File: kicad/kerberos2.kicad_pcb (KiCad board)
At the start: 2 copper layers, 62.5 x 83.8 mm, 212 parts, among them J1 5V, J10 rp_spare3, J11 rp_spare4, J12 rp_spare5, J13 rp_spare6, J14 503398-1892, J15 fpga_spare, J16 MIDI-in, J17 MIDI-thru, J18 MIDI-out, J19 IEC, J2 3.3V, J20 IEC, J21 IEC, J3 1.2V, J4 GND, J5 SWCLK, J6 SWD, J7 xout, J8 rp_spare1, J9 rp_spare2, Q1 Q_NMOS_GSD, Q10 Q_NMOS_GSD, Q11 Q_NMOS_GSD, Q12 Q_NMOS_GSD, Q13 Q_NMOS_GSD, Q2 Q_NMOS_GSD, Q3 Q_NMOS_GSD, Q4 Q_NMOS_GSD, Q5 Q_NMOS_GSD, Q6 Q_NMOS_GSD, Q7 Q_NMOS_GSD, Q8 Q_NMOS_GSD, Q9 Q_NMOS_GSD, SW1 side-button, SW2 SKRPADE010, U1 MX25L25645G, U10 M3406, U11 6N138, U12 74LS14, U2 MX25L25645G, U3 RP2040, U4 74ALVC164245DGG,51, U5 74ALVC164245DGG,51, U6 GW1NR-4&4B_QN881, U7 AD8694ARZ, U8 TMCS1108A3UQDR, U9 M3406, X1 SX3M12.000M20F30TNN

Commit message: circuit improvements fixed the level shifter circuit, added the shield pins to the reset button, and replaced the IEC circuit with unused pins of the 16 bit level shifter, and a new 6 channel open collector driver
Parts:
- removed the J10 at (202.5, 98.7)
- removed the J15 at (236.5, 103.2)
- removed the J19 at (163.3, 110.2)
- removed the J20 at (180.6, 110.2)
- removed the J21 at (197.9, 107.3)
- removed the J8 at (197.9, 98.7)
- removed Q1, Q10, Q11, Q12, Q13, Q2, Q3, Q4, Q5, Q6, Q7, Q8, Q9: Q_NMOS_GSD, Package_DFN_QFN:Diodes_DFN1006-3
- removed the R10 at (90.8, 28.9)
- removed the R11 at (95.5, 24.7)
- removed the R12 at (95.5, 21.8)
- removed the R17 at (99.9, 21.8)
- removed the R18 at (104.0, 27.6)
- removed the R19 at (108.7, 24.7)
- removed the R20 at (99.6, 30.6)
- removed the R21 at (95.2, 27.6)
- removed the R22 at (108.7, 21.8)
- removed the R28 at (178.0, 97.5)
- removed the R29 at (178.0, 91.5)
- removed the R30 at (182.4, 97.4)
- removed the R31 at (167.7, 102.1)
- removed the R32 at (182.4, 94.5)
- removed the R34 at (178.0, 88.6)
- removed the R38 at (216.1, 94.5)
- removed the R39 at (216.3, 91.5)
- removed the R40 at (211.7, 93.2)
- removed the R41 at (207.1, 97.9)
- removed the R42 at (216.3, 88.6)
- removed the R43 at (211.5, 97.9)
- removed R59, R74, R75, R76, R77, R78, R79, R80, R81, R82, R83, R85, R87, R89, R91, R93: 10k, Resistor_SMD:R_0805_2012Metric
- removed R72: 1k8, Resistor_SMD:R_0805_2012Metric
- removed R73: 3k3, Resistor_SMD:R_0805_2012Metric
- removed R84, R88, R92: 27, Resistor_SMD:R_0805_2012Metric
- removed R86, R90, R94: 22k, Resistor_SMD:R_0805_2012Metric
- added C18: 100n, Capacitor_SMD:C_0805_2012Metric, F.Cu at (1.70, 34.0)
- added C19: 100n, Capacitor_SMD:C_0805_2012Metric, F.Cu at (-8.13, 36.2)
- added C35: 100n, Capacitor_SMD:C_0805_2012Metric, F.Cu at (-2.75, 34.0)
- added C36: 100n, Capacitor_SMD:C_0805_2012Metric, F.Cu at (-12.6, 36.2)
- added J14: rp_spare4, Connector_PinHeader_2.54mm:PinHeader_1x01_P2.54mm_Vertical, F.Cu at (137.2, 18.4)
- added J2: IEC_ATN, Connector_PinHeader_2.54mm:PinHeader_1x01_P2.54mm_Vertical, F.Cu at (33.6, 23.4)
- added J3: IEC_SRQ, Connector_PinHeader_2.54mm:PinHeader_1x01_P2.54mm_Vertical, F.Cu at (29.0, 23.4)
- added J4: IEC_CLK, Connector_PinHeader_2.54mm:PinHeader_1x01_P2.54mm_Vertical, F.Cu at (24.3, 23.4)
- added J5: IEC_DAT, Connector_PinHeader_2.54mm:PinHeader_1x01_P2.54mm_Vertical, F.Cu at (29.0, 28.0)
- added J6: GND, Connector_PinHeader_2.54mm:PinHeader_1x01_P2.54mm_Vertical, F.Cu at (24.3, 28.0)
- added LOGO1: logo, Symbol:WEEE-Logo_4.2x6mm_SilkScreen, F.Cu at (86.0, 43.1)
- added LOGO2: logo, Symbol:CE-Logo_8.5x6mm_SilkScreen, F.Cu at (67.4, 42.5)
- added R3: 3k3, Resistor_SMD:R_0805_2012Metric, F.Cu at (42.6, 22.5)
- added R36: NA, Resistor_SMD:R_0805_2012Metric, F.Cu at (147.9, 27.4)
- added R37: 10k, Resistor_SMD:R_0805_2012Metric, F.Cu at (127.8, 30.8)
- added R4: 3k3, Resistor_SMD:R_0805_2012Metric, F.Cu at (24.2, 31.8)
- added R5: 3k3, Resistor_SMD:R_0805_2012Metric, F.Cu at (37.9, 28.4)
- added R6: 3k3, Resistor_SMD:R_0805_2012Metric, F.Cu at (33.5, 27.2)
- added U4: 74LCX16245, SOP50:SOP50P810X120-48N, F.Cu at (93.2, 99.5)
- added U8: 74LS06, Package_SO:SO-14_3.9x8.65mm_P1.27mm, F.Cu at (-0.75, 26.8)
- added U9: 74LS06, Package_SO:SO-14_3.9x8.65mm_P1.27mm, F.Cu at (7.70, 26.8)
- J11: value rp_spare4 -> rp_spare1
- J12: value rp_spare5 -> rp_spare2
- J13: value rp_spare6 -> rp_spare3
- J9: value rp_spare2 -> current-measurement
- R23, R24, R25, R26, R27, R33: value 27 -> 10k
- SW1: value side-button -> side-switch
- U1: moved to B.Cu
- U5: renamed from U4; value 74ALVC164245DGG,51 -> 74LCX16245; footprint Package_SO:TSSOP-48_8x12.5mm_P0.5mm -> SOP50:SOP50P810X120-48N
- U7: renamed from U5; value 74ALVC164245DGG,51 -> 74LCX16245; footprint Package_SO:TSSOP-48_8x12.5mm_P0.5mm -> SOP50:SOP50P810X120-48N
- moved R25 198.2 mm to (-3.70, 37.0)
- moved R27 188.9 mm to (0.71, 37.0)
- moved R26 187.1 mm to (14.1, 22.5)
- moved R23 178.9 mm to (14.1, 25.5)
- moved R24 178.1 mm to (6.13, 34.0)
- moved R15 159.8 mm to (28.6, 31.8)
- moved J11 109.6 mm to (127.9, 18.4)
- moved U2 97.2 mm to (75.7, 61.9)
- moved J12 96.5 mm to (132.6, 18.4)
- moved J13 96.4 mm to (132.6, 23.1)
- moved C10 89.7 mm to (134.4, 119.1)
- moved C15 89.7 mm to (134.4, 116.1)
- moved C5 89.7 mm to (121.0, 123.4)
- moved C7 89.7 mm to (121.0, 120.4)
- moved C8 89.7 mm to (125.4, 123.3)
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- renumbered C3 to C2, C19 to C20, C20 to C24, C18 to C25, C25 to C26, C2 to C3, C24 to C30, C26 to C31, C30 to C32, C31 to C33, C32 to C34, C33 to C37, C34 to C38, C35 to C39, C36 to C40, C37 to C41, C38 to C42, C39 to C43, C40 to C44, C41 to C45, C42 to C46, C43 to C47, J4 to J10, J5 to J15, J6 to J16, J7 to J17, J14 to J18, J16 to J19, J17 to J20, J18 to J21, J2 to J7, J3 to J8, R5 to R10, R6 to R11, R3 to R12, R9 to R17, R35 to R18, R36 to R19, R37 to R20, R44 to R21, R45 to R22, R46 to R28, R47 to R29, R49 to R30, R50 to R31, R48 to R32, R51 to R34, R52 to R35, R53 to R38, R54 to R39, R55 to R40, R56 to R41, R57 to R42, R58 to R43, R60 to R44, R61 to R45, R62 to R46, R63 to R47, R64 to R48, R65 to R49, R66 to R50, R67 to R51, R68 to R52, R69 to R53, R70 to R54, R71 to R55, R4 to R7, R7 to R8, R8 to R9, U7 to U10, U8 to U11, U9 to U12, U10 to U13, U11 to U14, U12 to U15
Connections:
- J18 pad 1: Net-(J14-Pad1) -> Net-(J18-Pad1)
- J18 pad 10: Net-(J14-Pad10) -> Net-(J18-Pad10)
- J18 pad 2: Net-(J14-Pad2) -> Net-(J18-Pad2)
- J18 pad 3: Net-(J14-Pad3) -> Net-(J18-Pad3)
- J18 pad 5: Net-(J14-Pad5) -> Net-(J18-Pad5)
- J18 pad 7: Net-(J14-Pad7) -> Net-(J18-Pad7)
- J18 pad 8: Net-(J14-Pad8) -> Net-(J18-Pad8)
- J9 pad 1: Net-(J9-Pad1) -> /current sense/Vout
- JP9 pad 1: Net-(JP9-Pad1) -> GND
- JP9 pad 2: GND -> Net-(JP9-Pad2)
- R13 pad 1: /RP2040 microcontroller/spare5 -> Net-(J2-Pad1)
- R13 pad 2: /GW1NR FPGA/spare5 -> /GW1NR FPGA/IEC_ATN
- R14 pad 1: /RP2040 microcontroller/spare6 -> Net-(J3-Pad1)
- R14 pad 2: /GW1NR FPGA/spare6 -> /GW1NR FPGA/IEC_SRQ
- R15 pad 1: /RP2040 microcontroller/spare7 -> Net-(J4-Pad1)
- R15 pad 2: /GW1NR FPGA/spare7 -> /GW1NR FPGA/IEC_CLK
- R16 pad 1: /RP2040 microcontroller/JTAGSEL_N -> Net-(J5-Pad1)
- R16 pad 2: /GW1NR FPGA/JTAGSEL_N -> /GW1NR FPGA/IEC_DAT
- R18 pad 2: Net-(R31-Pad2) -> /GW1NR FPGA/FLASH-CS
- R19 pad 2: Net-(R36-Pad2) -> Net-(R19-Pad2)
- R21 pad 2: Net-(JP9-Pad1) -> Net-(JP9-Pad2)
- R22 pad 1: Net-(J14-Pad10) -> Net-(J18-Pad10)
- R23 pad 1: /RP2040 microcontroller/FLASH-SIO1 -> GND
- R24 pad 1: /RP2040 microcontroller/FLASH-SIO0 -> GND
- R25 pad 1: /RP2040 microcontroller/FLASH-SCLK -> GND
- R26 pad 1: /RP2040 microcontroller/FLASH-CS -> GND
- R27 pad 1: /RP2040 microcontroller/FLASH-SIO2 -> GND
- R33 pad 1: /GW1NR FPGA/FLASH-SIO3 -> +3.3V
- R33 pad 2: Net-(R33-Pad2) -> /GW1NR FPGA/FLASH-SIO3
- R34 pad 1: Net-(R51-Pad1) (its old number) -> GND
- R34 pad 2: GND -> Net-(R34-Pad2)
- R35 pad 1: Net-(R52-Pad1) (its old number) -> GND
- R35 pad 2: GND -> Net-(R35-Pad2)
- RN1 pad 1: Net-(JP1-Pad8) -> Net-(JP1-Pad4)
- RN1 pad 10: /~{DMA} -> I/O2
- RN1 pad 11: /BA -> ~{EXROM}
- RN1 pad 12: /~{IRQ} -> ~{GAME}
- RN1 pad 13: /R/W -> I/O1
- RN1 pad 14: /DOT-CLK -> DOT-CLK
- RN1 pad 15: /I/O1 -> R/W
- RN1 pad 16: /~{GAME} -> ~{IRQ}
- RN1 pad 2: Net-(JP1-Pad7) -> Net-(JP1-Pad5)
- RN1 pad 4: Net-(JP1-Pad5) -> Net-(JP1-Pad7)
- RN1 pad 5: Net-(JP1-Pad4) -> Net-(JP1-Pad8)
- RN1 pad 6: Net-(JP1-Pad12) -> Net-(JP1-Pad9)
- RN1 pad 7: Net-(JP1-Pad13) -> Net-(JP1-Pad10)
- RN1 pad 8: Net-(JP1-PadE) -> Net-(JP1-Pad11)
- RN1 pad 9: /S02 -> ~{ROML}
- RN2 pad 1: unconnected-(RN2-Pad1) -> Net-(JP1-Pad12)
- RN2 pad 10: /I/O2 -> unconnected-(RN2-Pad10)
- RN2 pad 11: /~{ROML} -> S02
- RN2 pad 12: /~{ROMH} -> ~{NMI}
- RN2 pad 13: /~{RESET} -> ~{RESET}
- RN2 pad 14: /~{NMI} -> ~{ROMH}
- RN2 pad 15: unconnected-(RN2-Pad15) -> ~{DMA}
- RN2 pad 16: unconnected-(RN2-Pad16) -> BA
- RN2 pad 2: unconnected-(RN2-Pad2) -> Net-(JP1-Pad13)
- RN2 pad 3: Net-(JP1-PadD) -> Net-(JP1-PadB)
- RN2 pad 5: Net-(JP1-PadB) -> Net-(JP1-PadD)
- RN2 pad 6: Net-(JP1-Pad11) -> Net-(JP1-PadE)
- RN2 pad 7: Net-(JP1-Pad10) -> unconnected-(RN2-Pad7)
- RN2 pad 8: Net-(JP1-Pad9) -> unconnected-(RN2-Pad8)
- RN2 pad 9: /~{EXROM} -> unconnected-(RN2-Pad9)
- RN3 pad 1: /A0 -> A0
- RN3 pad 2: /A1 -> A1
- RN3 pad 3: /A2 -> A2
- RN3 pad 4: /A3 -> A3
- RN3 pad 5: /A4 -> A4
- RN3 pad 6: /A5 -> A5
- RN3 pad 7: /A6 -> A6
- RN3 pad 8: /A7 -> A7
- RN4 pad 1: /A8 -> A8
- RN4 pad 2: /A9 -> A9
- RN4 pad 3: /A10 -> A10
- RN4 pad 4: /A11 -> A11
- RN4 pad 5: /A12 -> A12
- RN4 pad 6: /A13 -> A13
- RN4 pad 7: /A14 -> A14
- RN4 pad 8: /A15 -> A15
- RN5 pad 1: /D0 -> D0
- RN5 pad 2: /D1 -> D1
- RN5 pad 3: /D2 -> D2
- RN5 pad 4: /D3 -> D3
- RN5 pad 5: /D4 -> D4
- RN5 pad 6: /D5 -> D5
- RN5 pad 7: /D6 -> D6
- RN5 pad 8: /D7 -> D7
- SW1 pad 2: Net-(R36-Pad2) -> Net-(R19-Pad2)
- SW1 pad S1: (no net) -> GND
- SW1 pad S2: (no net) -> GND
- U1 pad 1: Net-(R31-Pad2) -> /GW1NR FPGA/FLASH-CS
- U1 pad 2: Net-(R34-Pad2) -> /GW1NR FPGA/FLASH-SIO1
- U1 pad 3: Net-(R32-Pad2) -> /GW1NR FPGA/FLASH-SIO2
- U1 pad 5: Net-(R29-Pad2) -> /GW1NR FPGA/FLASH-SIO0
- U1 pad 6: Net-(R30-Pad2) -> /GW1NR FPGA/FLASH-SCLK
- U1 pad 7: Net-(R33-Pad2) -> /GW1NR FPGA/FLASH-SIO3
- U15 pad 12: Net-(R72-Pad2) -> /GW1NR FPGA/MIDI-in
- U2 pad 1: Net-(R26-Pad2) -> /RP2040 microcontroller/FLASH-CS
- U2 pad 2: Net-(R23-Pad2) -> /RP2040 microcontroller/FLASH-SIO1
- U2 pad 3: Net-(R27-Pad2) -> /RP2040 microcontroller/FLASH-SIO2
- U2 pad 5: Net-(R24-Pad2) -> /RP2040 microcontroller/FLASH-SIO0
- U2 pad 6: Net-(R25-Pad2) -> /RP2040 microcontroller/FLASH-SCLK
- U2 pad 7: Net-(R28-Pad2) -> /RP2040 microcontroller/FLASH-SIO3
- U3 pad 11: /RP2040 microcontroller/spare2 -> Net-(J11-Pad1)
- U3 pad 12: /RP2040 microcontroller/spare3 -> Net-(J12-Pad1)
- U3 pad 13: /RP2040 microcontroller/spare4 -> Net-(J13-Pad1)
- U3 pad 14: /RP2040 microcontroller/spare5 -> Net-(J14-Pad1)
- U3 pad 15: /RP2040 microcontroller/spare6 -> /GW1NR FPGA/IEC_CLK_d
- U3 pad 16: Net-(R36-Pad2) -> /GW1NR FPGA/IEC_DAT_d
- U3 pad 17: /RP2040 microcontroller/spare7 -> Net-(R19-Pad2)
- U3 pad 2: /RP2040 microcontroller/JTAGSEL_N -> /GW1NR FPGA/JTAGSEL_N
- U3 pad 28: Net-(J8-Pad1) -> Net-(J18-Pad3)
- U3 pad 29: Net-(J9-Pad1) -> Net-(J18-Pad5)
- U3 pad 3: /RP2040 microcontroller/TCK -> /GW1NR FPGA/TCK
- U3 pad 30: Net-(J14-Pad3) -> Net-(J18-Pad7)
- U3 pad 31: Net-(J14-Pad5) -> Net-(J18-Pad8)
- U3 pad 32: Net-(J14-Pad7) -> Net-(J18-Pad1)
- U3 pad 34: Net-(J14-Pad8) -> Net-(J18-Pad2)
- U3 pad 35: Net-(J14-Pad1) -> Net-(J18-Pad10)
- U3 pad 36: Net-(J14-Pad2) -> /GW1NR FPGA/IEC_ATN_t
- U3 pad 37: Net-(J14-Pad10) -> /GW1NR FPGA/IEC_SRQ_t
- U3 pad 38: Net-(J10-Pad1) -> /GW1NR FPGA/IEC_CLK_t
- U3 pad 39: Net-(J11-Pad1) -> /GW1NR FPGA/IEC_DAT_t
- U3 pad 4: /RP2040 microcontroller/TMS -> /GW1NR FPGA/TMS
- U3 pad 40: Net-(J12-Pad1) -> /GW1NR FPGA/IEC_ATN_d
- U3 pad 41: Net-(J13-Pad1) -> /GW1NR FPGA/IEC_SRQ_d
- U3 pad 5: /RP2040 microcontroller/TDO -> /GW1NR FPGA/TDO
- U3 pad 6: /RP2040 microcontroller/TDI -> /GW1NR FPGA/TDI
- U3 pad 7: /RP2040 microcontroller/DONE -> /GW1NR FPGA/DONE
- U3 pad 8: /RP2040 microcontroller/RECONFIG_N -> /GW1NR FPGA/RECONFIG_N
- U5 pad 11: /GW1NR FPGA/A6 -> A9
- U5 pad 12: /GW1NR FPGA/A7 -> A8
- U5 pad 13: /GW1NR FPGA/A8 -> A7
- U5 pad 14: /GW1NR FPGA/A9 -> A6
- U5 pad 16: /GW1NR FPGA/A10 -> A5
- U5 pad 17: /GW1NR FPGA/A11 -> A4
- U5 pad 19: /GW1NR FPGA/A12 -> A3
- U5 pad 2: /GW1NR FPGA/A0 -> A15
- U5 pad 20: /GW1NR FPGA/A13 -> A2
- U5 pad 22: /GW1NR FPGA/A14 -> A1
- U5 pad 23: /GW1NR FPGA/A15 -> A0
- U5 pad 26: /GW1NR FPGA/A15_t -> /GW1NR FPGA/A0_t
- U5 pad 27: /GW1NR FPGA/A14_t -> /GW1NR FPGA/A1_t
- U5 pad 29: /GW1NR FPGA/A13_t -> /GW1NR FPGA/A2_t
- U5 pad 3: /GW1NR FPGA/A1 -> A14
- U5 pad 30: /GW1NR FPGA/A12_t -> /GW1NR FPGA/A3_t
- U5 pad 32: /GW1NR FPGA/A11_t -> /GW1NR FPGA/A4_t
- U5 pad 33: /GW1NR FPGA/A10_t -> /GW1NR FPGA/A5_t
- U5 pad 35: /GW1NR FPGA/A9_t -> /GW1NR FPGA/A6_t
- U5 pad 36: /GW1NR FPGA/A8_t -> /GW1NR FPGA/A7_t
- U5 pad 37: /GW1NR FPGA/A7_t -> /GW1NR FPGA/A8_t
- U5 pad 38: /GW1NR FPGA/A6_t -> /GW1NR FPGA/A9_t
- U5 pad 40: /GW1NR FPGA/A5_t -> /GW1NR FPGA/A10_t
- U5 pad 41: /GW1NR FPGA/A4_t -> /GW1NR FPGA/A11_t
- U5 pad 43: /GW1NR FPGA/A3_t -> /GW1NR FPGA/A12_t
- U5 pad 44: /GW1NR FPGA/A2_t -> /GW1NR FPGA/A13_t
- U5 pad 46: /GW1NR FPGA/A1_t -> /GW1NR FPGA/A14_t
- U5 pad 47: /GW1NR FPGA/A0_t -> /GW1NR FPGA/A15_t
- U5 pad 5: /GW1NR FPGA/A2 -> A13
- U5 pad 6: /GW1NR FPGA/A3 -> A12
- U5 pad 8: /GW1NR FPGA/A4 -> A11
- U5 pad 9: /GW1NR FPGA/A5 -> A10
- U6 pad 13: /GW1NR FPGA/FLASH-SCLK -> /GW1NR FPGA/~{ROML_d}
- U6 pad 14: /GW1NR FPGA/MIDI-thru -> /GW1NR FPGA/~{ROMH_d}
- U6 pad 15: /GW1NR FPGA/MIDI-out -> /GW1NR FPGA/~{RESET_d}
- U6 pad 16: /GW1NR FPGA/MIDI-in -> /GW1NR FPGA/~{NMI_d}
- U6 pad 17: /GW1NR FPGA/A0_t -> /GW1NR FPGA/~{EXROM_d}
- U6 pad 18: /GW1NR FPGA/A1_t -> /GW1NR FPGA/~{GAME_d}
- U6 pad 19: /GW1NR FPGA/A2_t -> /GW1NR FPGA/R/W_d
- U6 pad 20: /GW1NR FPGA/A3_t -> /GW1NR FPGA/~{IRQ_d}
- U6 pad 25: /GW1NR FPGA/A4_t -> /GW1NR FPGA/MIDI-thru
- U6 pad 26: /GW1NR FPGA/A5_t -> /GW1NR FPGA/MIDI-out
- U6 pad 27: /GW1NR FPGA/A6_t -> /GW1NR FPGA/MIDI-in_t
- U6 pad 28: /GW1NR FPGA/A7_t -> /GW1NR FPGA/A15_t
- U6 pad 29: /GW1NR FPGA/A8_t -> /GW1NR FPGA/A14_t
- U6 pad 3: Net-(J15-Pad1) (its old number) -> /GW1NR FPGA/spare1
- U6 pad 30: /GW1NR FPGA/A9_t -> /GW1NR FPGA/A13_t
- U6 pad 31: /GW1NR FPGA/A10_t -> /GW1NR FPGA/A12_t
- U6 pad 33: /GW1NR FPGA/A12_t -> /GW1NR FPGA/A10_t
- U6 pad 34: /GW1NR FPGA/A13_t -> /GW1NR FPGA/A9_t
- U6 pad 35: /GW1NR FPGA/A14_t -> /GW1NR FPGA/A8_t
- U6 pad 36: /GW1NR FPGA/A15_t -> /GW1NR FPGA/A7_t
- U6 pad 37: /GW1NR FPGA/S02_t -> /GW1NR FPGA/A6_t
- U6 pad 38: /GW1NR FPGA/BA_t -> /GW1NR FPGA/A5_t
- U6 pad 39: /GW1NR FPGA/DIR_A -> /GW1NR FPGA/A4_t
- U6 pad 40: /GW1NR FPGA/DIR_D -> /GW1NR FPGA/A3_t
- U6 pad 41: /GW1NR FPGA/R/W_t -> /GW1NR FPGA/A2_t
- U6 pad 42: /GW1NR FPGA/DOT-CLK_t -> /GW1NR FPGA/A1_t
- U6 pad 47: /GW1NR FPGA/I/O1_t -> /GW1NR FPGA/A0_t
- U6 pad 48: /GW1NR FPGA/~{NMI_t} -> /GW1NR FPGA/S02_t
- U6 pad 49: /GW1NR FPGA/~{RESET_t} -> /GW1NR FPGA/BA_t
- U6 pad 50: /GW1NR FPGA/A14_down -> /GW1NR FPGA/DIR_A
- U6 pad 51: /GW1NR FPGA/FLASH-SIO0 -> /GW1NR FPGA/DIR_D
- U6 pad 52: /GW1NR FPGA/FLASH-SIO1 -> /GW1NR FPGA/R/W_t
- U6 pad 53: /GW1NR FPGA/FLASH-SIO2 -> /GW1NR FPGA/DOT-CLK_t
- U6 pad 54: /GW1NR FPGA/FLASH-SIO3 -> /GW1NR FPGA/I/O1_t
- U6 pad 55: /GW1NR FPGA/spare6 -> /GW1NR FPGA/I/O2_t
- U6 pad 56: /GW1NR FPGA/spare5 -> /GW1NR FPGA/FLASH-SIO2
- U6 pad 57: /GW1NR FPGA/spare4 -> /GW1NR FPGA/FLASH-SIO3
- U6 pad 59: /GW1NR FPGA/spare7 -> /GW1NR FPGA/FLASH-SCLK
- U6 pad 61: /GW1NR FPGA/spare3 -> /GW1NR FPGA/FLASH-SIO0
- U6 pad 62: /GW1NR FPGA/spare2 -> /GW1NR FPGA/FLASH-SIO1
- U6 pad 63: /GW1NR FPGA/spare1 -> /GW1NR FPGA/~{DMA_d}
- U6 pad 68: /GW1NR FPGA/~{ROMH_t} -> /GW1NR FPGA/D7_t
- U6 pad 69: /GW1NR FPGA/~{ROML_t} -> /GW1NR FPGA/D6_t
- U6 pad 70: /GW1NR FPGA/~{EXROM_t} -> /GW1NR FPGA/D5_t
- U6 pad 71: /GW1NR FPGA/~{GAME_t} -> /GW1NR FPGA/D4_t
- U6 pad 72: /GW1NR FPGA/R/W_t -> /GW1NR FPGA/D3_t
- U6 pad 73: /GW1NR FPGA/~{IRQ_t} -> /GW1NR FPGA/D2_t
- U6 pad 74: /GW1NR FPGA/~{DMA_t} -> /GW1NR FPGA/D1_t
- U6 pad 75: /GW1NR FPGA/D7_t -> /GW1NR FPGA/D0_t
- U6 pad 76: /GW1NR FPGA/D6_t -> /GW1NR FPGA/~{ROMH_t}
- U6 pad 77: /GW1NR FPGA/D5_t -> /GW1NR FPGA/~{ROML_t}
- U6 pad 79: /GW1NR FPGA/D4_t -> /GW1NR FPGA/~{EXROM_t}
- U6 pad 80: /GW1NR FPGA/D3_t -> /GW1NR FPGA/~{GAME_t}
- U6 pad 81: /GW1NR FPGA/D2_t -> /GW1NR FPGA/R/W_t
- U6 pad 82: /GW1NR FPGA/D1_t -> /GW1NR FPGA/~{IRQ_t}
- U6 pad 83: /GW1NR FPGA/D0_t -> /GW1NR FPGA/~{DMA_t}
- U6 pad 84: /GW1NR FPGA/~{ROMH_t} -> /GW1NR FPGA/~{RESET_t}
- U6 pad 85: /GW1NR FPGA/~{ROML_t} -> /GW1NR FPGA/~{NMI_t}
- U6 pad 86: /GW1NR FPGA/I/O2_t -> /GW1NR FPGA/A14_d
- U6 pad 87: Net-(R51-Pad1) (its old number) -> Net-(R34-Pad2)
- U6 pad 88: Net-(R52-Pad1) (its old number) -> Net-(R35-Pad2)
- U7 pad 1: /GW1NR FPGA/DIR_D -> GND
- U7 pad 11: /GW1NR FPGA/D6 -> ~{ROML}
- U7 pad 12: /GW1NR FPGA/D7 -> ~{ROMH}
- U7 pad 13: /GW1NR FPGA/S02 -> D7
- U7 pad 14: /GW1NR FPGA/BA -> D6
- U7 pad 16: /GW1NR FPGA/R/W -> D5
- U7 pad 17: /GW1NR FPGA/DOT-CLK -> D4
- U7 pad 19: /GW1NR FPGA/I/O1 -> D3
- U7 pad 2: /GW1NR FPGA/D0 -> S02
- U7 pad 20: /GW1NR FPGA/I/O2 -> D2
- U7 pad 22: /GW1NR FPGA/~{ROML} -> D1
- U7 pad 23: /GW1NR FPGA/~{ROMH} -> D0
- U7 pad 24: GND -> /GW1NR FPGA/DIR_D
- U7 pad 26: /GW1NR FPGA/~{ROMH_t} -> /GW1NR FPGA/D0_t
- U7 pad 27: /GW1NR FPGA/~{ROML_t} -> /GW1NR FPGA/D1_t
- U7 pad 29: /GW1NR FPGA/I/O2_t -> /GW1NR FPGA/D2_t
- U7 pad 3: /GW1NR FPGA/D1 -> BA
- U7 pad 30: /GW1NR FPGA/I/O1_t -> /GW1NR FPGA/D3_t
- U7 pad 32: /GW1NR FPGA/DOT-CLK_t -> /GW1NR FPGA/D4_t
- U7 pad 33: /GW1NR FPGA/R/W_t -> /GW1NR FPGA/D5_t
- U7 pad 35: /GW1NR FPGA/BA_t -> /GW1NR FPGA/D6_t
- U7 pad 36: /GW1NR FPGA/S02_t -> /GW1NR FPGA/D7_t
- U7 pad 37: /GW1NR FPGA/D7_t -> /GW1NR FPGA/~{ROMH_t}
- U7 pad 38: /GW1NR FPGA/D6_t -> /GW1NR FPGA/~{ROML_t}
- U7 pad 40: /GW1NR FPGA/D5_t -> /GW1NR FPGA/I/O2_t
- U7 pad 41: /GW1NR FPGA/D4_t -> /GW1NR FPGA/I/O1_t
- U7 pad 43: /GW1NR FPGA/D3_t -> /GW1NR FPGA/DOT-CLK_t
- U7 pad 44: /GW1NR FPGA/D2_t -> /GW1NR FPGA/R/W_t
- U7 pad 46: /GW1NR FPGA/D1_t -> /GW1NR FPGA/BA_t
- U7 pad 47: /GW1NR FPGA/D0_t -> /GW1NR FPGA/S02_t
- U7 pad 5: /GW1NR FPGA/D2 -> R/W
- U7 pad 6: /GW1NR FPGA/D3 -> DOT-CLK
- U7 pad 8: /GW1NR FPGA/D4 -> I/O1
- U7 pad 9: /GW1NR FPGA/D5 -> I/O2

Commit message: started routing
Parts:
- C1, C11, C12, C14, C15, C16, C18, C19, C2, C20, C21, C22, C23, C24, C25, C26, C27, C28, C29, C3, C30, C31, C32, C33, C34, C35, C36, C37, C38, C39, C44, C45, C46, C5, C6, C7, C8, C9, D5, D6, D7, FB1, R12, R23, R24, R25, R26, R27, R37, R7, U10, U11, U2, U8, U9, X1: moved to B.Cu
- R1, R2: value 5.1 -> 5k1
- R42: renamed from R38; moved to B.Cu
- R43: renamed from R39; moved to B.Cu
- R44: renamed from R40; moved to B.Cu
- R45: renamed from R41; moved to B.Cu
- R46: renamed from R42; moved to B.Cu
- R47: renamed from R43; moved to B.Cu
- R52: renamed from R48; footprint Resistor_SMD:R_0805_2012Metric -> Resistor_SMD:R_1206_3216Metric
- R53: renamed from R49; footprint Resistor_SMD:R_0805_2012Metric -> Resistor_SMD:R_1206_3216Metric; moved to B.Cu
- R54: renamed from R50; footprint Resistor_SMD:R_0805_2012Metric -> Resistor_SMD:R_1206_3216Metric; moved to B.Cu
- R55: renamed from R51; footprint Resistor_SMD:R_0805_2012Metric -> Resistor_SMD:R_1206_3216Metric; moved to B.Cu
- R56: renamed from R52; footprint Resistor_SMD:R_0805_2012Metric -> Resistor_SMD:R_1206_3216Metric; moved to B.Cu
- R57: renamed from R53; moved to B.Cu
- R58: renamed from R54; footprint Resistor_SMD:R_0805_2012Metric -> Resistor_SMD:R_1206_3216Metric
- R59: renamed from R55; footprint Resistor_SMD:R_0805_2012Metric -> Resistor_SMD:R_1206_3216Metric
- moved C39 136.9 mm to (47.0, 88.5), turned to 90 degrees
- moved R47 132.4 mm to (51.6, 94.1), turned to 180 degrees
- moved C36 130.9 mm to (105.3, 93.2), turned to -90 degrees
- moved J9 128.4 mm to (54.3, 99.8)
- moved R46 125.8 mm to (57.1, 92.9), turned to -90 degrees
- moved R43 125.1 mm to (56.3, 81.4)
- moved C37 121.5 mm to (57.4, 87.4)
- moved U8 120.2 mm to (99.4, 93.2), turned to 90 degrees
- moved R44 119.8 mm to (58.1, 89.7), turned to 180 degrees
- moved C38 118.9 mm to (52.1, 81.4), turned to 180 degrees
- moved R42 118.3 mm to (57.4, 84.5), turned to 90 degrees
- moved C18 117.5 mm to (95.9, 104.1)
- moved R45 117.3 mm to (60.0, 84.5), turned to -90 degrees
- moved R25 116.9 mm to (93.8, 101.4), turned to -90 degrees
- moved R27 116.8 mm to (98.2, 101.3), turned to -90 degrees
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- renumbered R44 to R48, R45 to R49, R46 to R50, R47 to R51
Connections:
- U3 pad 36: /GW1NR FPGA/IEC_ATN_t -> /GW1NR FPGA/IEC_DAT_t
- U3 pad 37: /GW1NR FPGA/IEC_SRQ_t -> /GW1NR FPGA/IEC_CLK_t
- U3 pad 38: /GW1NR FPGA/IEC_CLK_t -> /GW1NR FPGA/IEC_ATN_t
- U3 pad 39: /GW1NR FPGA/IEC_DAT_t -> /GW1NR FPGA/IEC_SRQ_t
- U6 pad 68: /GW1NR FPGA/D7_t -> /GW1NR FPGA/~{ROML_t}
- U6 pad 69: /GW1NR FPGA/D6_t -> /GW1NR FPGA/~{ROMH_t}
- U6 pad 70: /GW1NR FPGA/D5_t -> /GW1NR FPGA/D7_t
- U6 pad 71: /GW1NR FPGA/D4_t -> /GW1NR FPGA/D6_t
- U6 pad 72: /GW1NR FPGA/D3_t -> /GW1NR FPGA/D5_t
- U6 pad 73: /GW1NR FPGA/D2_t -> /GW1NR FPGA/D4_t
- U6 pad 74: /GW1NR FPGA/D1_t -> /GW1NR FPGA/D3_t
- U6 pad 75: /GW1NR FPGA/D0_t -> /GW1NR FPGA/D2_t
- U6 pad 76: /GW1NR FPGA/~{ROMH_t} -> /GW1NR FPGA/D1_t
- U6 pad 77: /GW1NR FPGA/~{ROML_t} -> /GW1NR FPGA/D0_t
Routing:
- net ~{RESET}: track 0.00 -> 48.4 mm, vias 0 -> 2
- net ~{NMI}: track 0.00 -> 39.6 mm, vias 0 -> 2
- net Net-(JP1-PadY): track 0.00 -> 38.5 mm, vias 0 -> 2
- net Net-(JP1-PadX): track 0.00 -> 35.8 mm, vias 0 -> 2
- net Net-(JP1-PadW): track 0.00 -> 32.9 mm, vias 0 -> 2
- net Net-(JP1-PadV): track 0.00 -> 32.0 mm, vias 0 -> 2
- net Net-(JP1-Pad13): track 0.00 -> 30.6 mm, vias 0 -> 2
- net Net-(JP1-Pad12): track 0.00 -> 28.8 mm, vias 0 -> 2
- net Net-(JP1-PadU): track 0.00 -> 28.7 mm, vias 0 -> 2
- net Net-(JP1-PadT): track 0.00 -> 26.7 mm, vias 0 -> 2
- net ~{ROMH}: track 0.00 -> 26.7 mm, vias 0 -> 2
- net Net-(JP1-PadS): track 0.00 -> 25.0 mm, vias 0 -> 2
- net Net-(JP1-Pad4): track 0.00 -> 24.4 mm
- net Net-(JP1-Pad21): track 0.00 -> 24.2 mm
- net Net-(JP1-Pad5): track 0.00 -> 23.6 mm
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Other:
- copper layers 2 -> 4

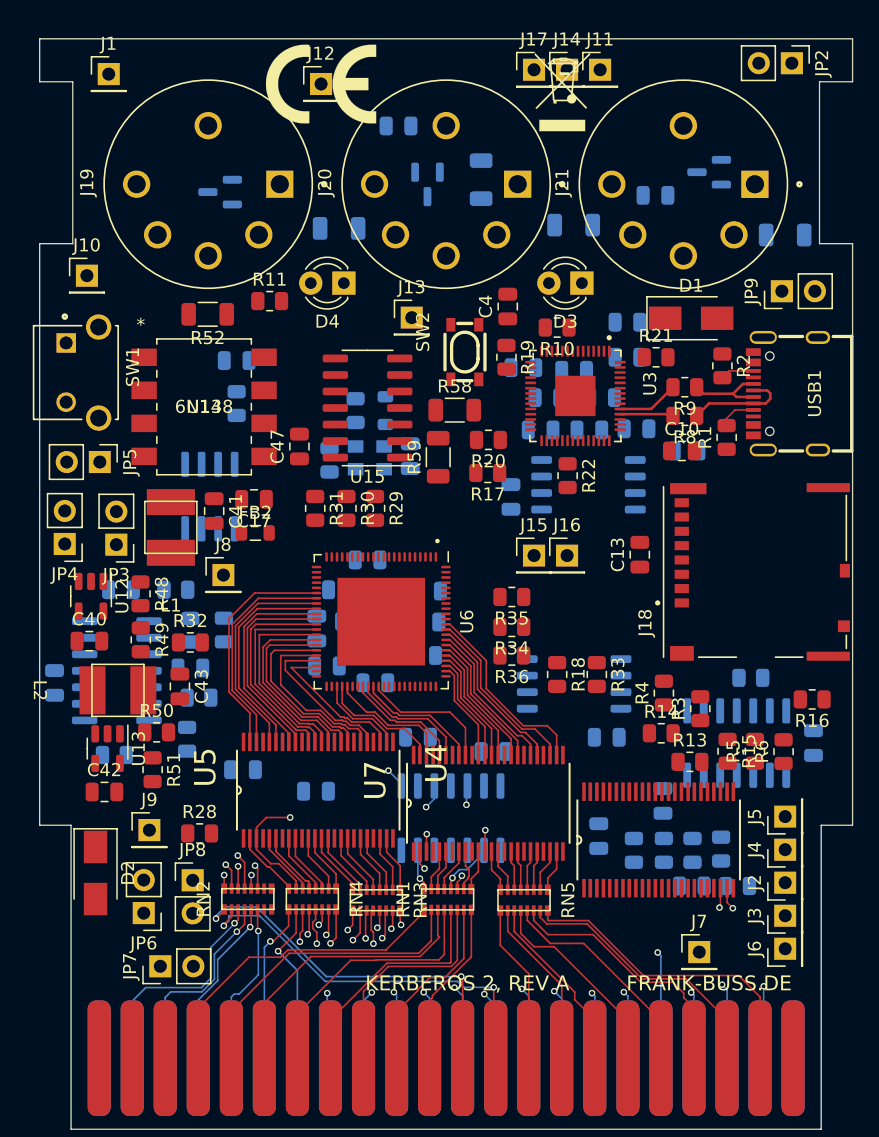
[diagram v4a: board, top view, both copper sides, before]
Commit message: board fully routed
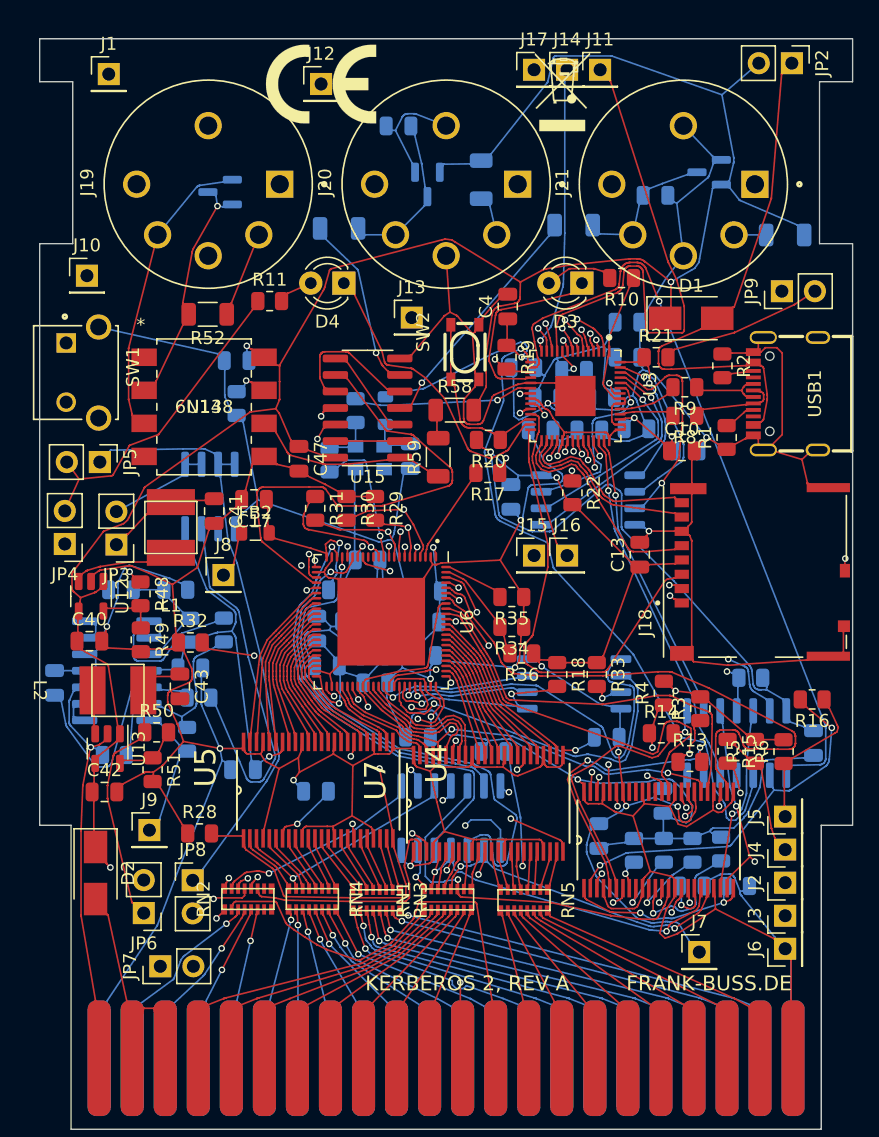
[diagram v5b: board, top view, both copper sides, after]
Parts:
- moved R10 6.25 mm to (90.6, 57.4)
- moved R22 1.37 mm to (86.8, 73.9)
- moved U2 1.17 mm to (88.0, 74.5)
- moved C47 0.94 mm to (65.8, 71.3), turned to -90 degrees
- moved R36 0.78 mm to (82.9, 86.3)
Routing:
- net GND: track 0.00 -> 729.7 mm, vias 0 -> 13
- net +3.3V: track 0.00 -> 388.4 mm, vias 0 -> 21
- net +5V: track 0.00 -> 292.0 mm, vias 0 -> 10
- net /GW1NR FPGA/IEC_DAT_d: track 0.00 -> 58.9 mm, vias 0 -> 1
- net /GW1NR FPGA/MIDI-in: track 0.00 -> 58.3 mm, vias 0 -> 2
- net Net-(C17-Pad1): track 0.00 -> 54.4 mm, vias 0 -> 4
- net /GW1NR FPGA/IEC_CLK_d: track 0.00 -> 51.0 mm, vias 0 -> 1
- net /current sense/sense-: track 0.00 -> 46.1 mm
- net /GW1NR FPGA/~{RESET_t}: track 0.00 -> 44.4 mm
- net /GW1NR FPGA/R/W_d: track 0.00 -> 41.0 mm, vias 0 -> 1
- net Net-(D1-Pad2): track 0.00 -> 40.8 mm
- net Net-(J11-Pad1): track 0.00 -> 40.2 mm
- net /GW1NR FPGA/~{GAME_d}: track 0.00 -> 40.0 mm, vias 0 -> 3
- net /GW1NR FPGA/MIDI-out: track 0.00 -> 38.4 mm
- net /GW1NR FPGA/MIDI-in_t: track 0.00 -> 38.1 mm, vias 0 -> 2
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
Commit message: changed hole clearance
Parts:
- R48: value 45k -> 45300
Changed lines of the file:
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@@
       (effects (font (size 1 1) (thickness 0.15)))
     )
-    (fp_text value "45k" (at 0 1.65 90) (layer "F.Fab")
+    (fp_text value "45300" (at 0 1.65 90) (layer "F.Fab")
       (effects (font (size 1 1) (thickness 0.15)))
     )

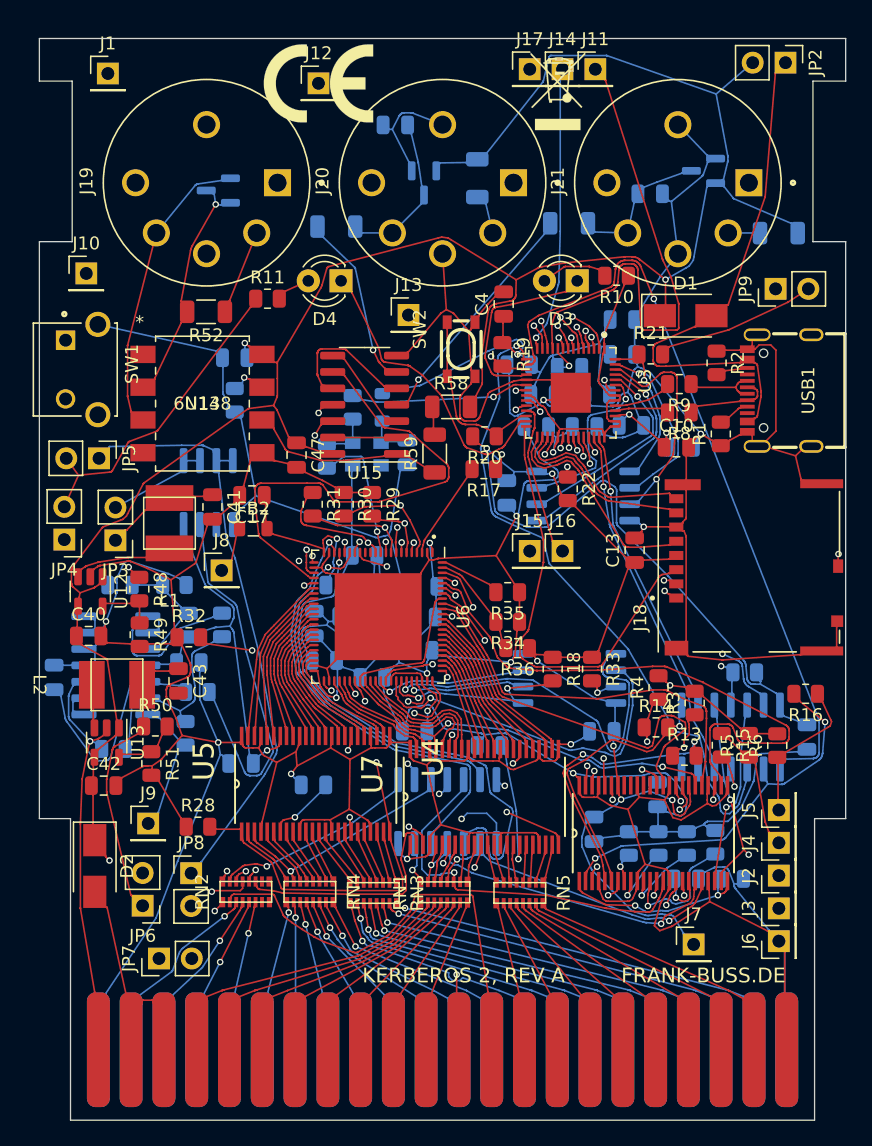
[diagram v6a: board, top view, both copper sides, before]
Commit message: footprint fixed and gerber files, as ordered at JLCPCB
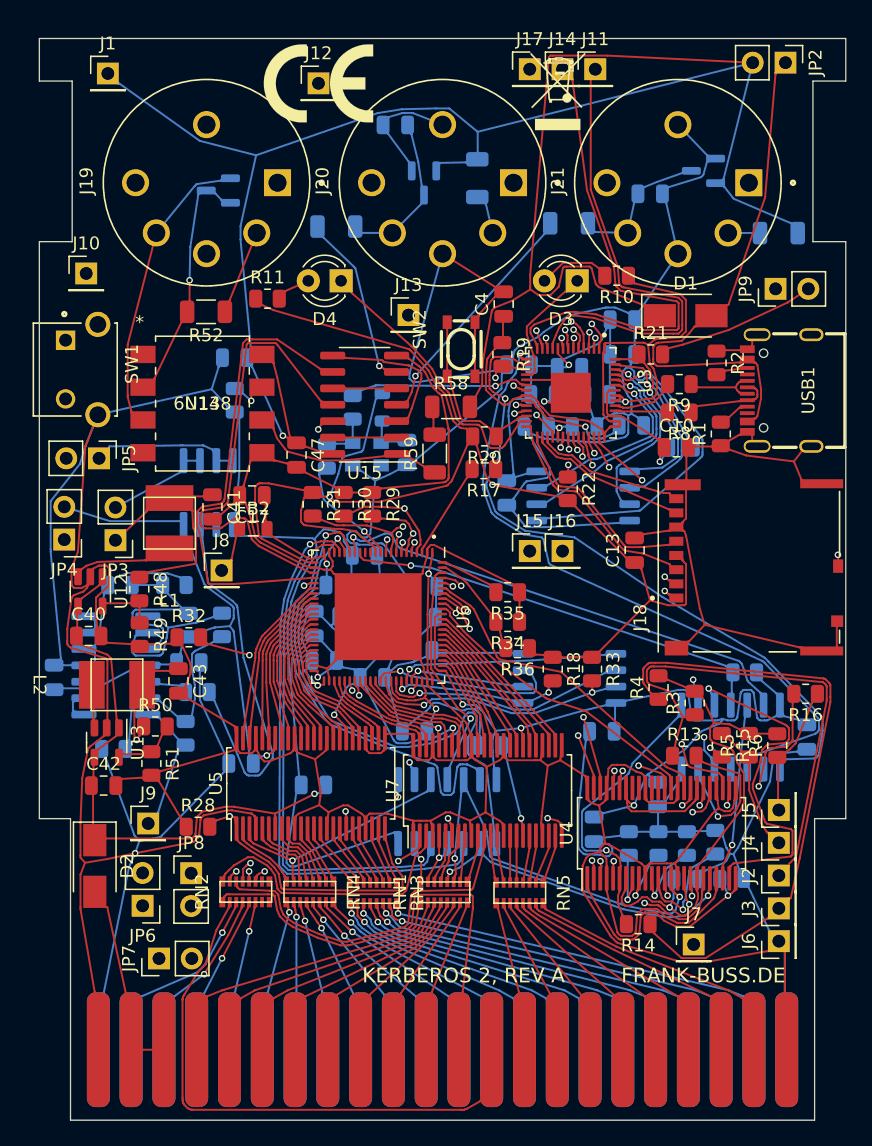
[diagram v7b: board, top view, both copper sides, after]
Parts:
- U4, U5, U7: footprint SOP50:SOP50P810X120-48N -> Package_SO:SSOP-48_5.3x12.8mm_P0.5mm
- moved R14 15.3 mm to (92.2, 107.7), turned to 180 degrees
- moved U4 0.63 mm to (94.0, 100.6)
- moved U7 0.55 mm to (80.5, 97.3)
- moved U5 0.39 mm to (66.8, 96.7)
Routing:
- net GND: track 729.7 -> 904.6 mm, vias 13 -> 2
- net +5V: track 292.0 -> 323.3 mm, vias 10 -> 6
- net Net-(J3-Pad1): track 20.1 -> 48.3 mm, vias 1 -> 0
- net Net-(J2-Pad1): track 16.6 -> 38.8 mm, vias 1 -> 0
- net /GW1NR FPGA/MIDI-thru: track 14.3 -> 35.6 mm, vias 2 -> 0
- net Net-(J18-Pad3): track 34.7 -> 17.5 mm
- net +3.3V: track 388.4 -> 405.3 mm, vias 21 -> 13
- net Net-(J14-Pad1): track 22.1 -> 38.4 mm, vias 1 -> 0
- net /GW1NR FPGA/~{RESET_t}: track 44.4 -> 29.4 mm, vias 0 -> 2
- net /GW1NR FPGA/FLASH-SIO0: track 29.4 -> 17.1 mm
- net Net-(C17-Pad1): track 54.4 -> 45.5 mm, vias 4 -> 3
- net Net-(JP1-Pad13): track 35.2 -> 44.0 mm
- net /GW1NR FPGA/FLASH-SCLK: track 27.6 -> 18.9 mm
- net /GW1NR FPGA/~{EXROM_t}: track 31.4 -> 23.2 mm
- net Net-(JP1-Pad12): track 28.1 -> 36.0 mm, vias 2 -> 0
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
